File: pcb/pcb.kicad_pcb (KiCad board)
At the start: 2 copper layers, 229.9 x 97.8 mm, 145 parts, among them J1 USB_C_Receptacle_USB2.0, SW1 Reset, SW10 SW_Push, SW11 SW_Push, SW12 SW_Push, SW13 SW_Push, SW14 SW_Push, SW15 SW_Push, SW16 SW_Push, SW17 SW_Push, SW18 SW_Push, SW19 SW_Push, SW2 SW_Push, SW20 SW_Push, SW21 SW_Push, SW22 SW_Push, SW23 SW_Push, SW24 SW_Push, SW25 SW_Push, SW26 SW_Push, SW27 SW_Push, SW28 SW_Push, SW29 SW_Push, SW3 SW_Push, SW30 SW_Push, SW31 SW_Push, SW32 SW_Push, SW33 SW_Push, SW34 SW_Push, SW35 SW_Push, SW36 SW_Push, SW37 SW_Push, SW38 SW_Push, SW39 SW_Push, SW4 SW_Push, SW40 SW_Push, SW41 SW_Push, SW42 SW_Push, SW43 SW_Push, SW44 SW_Push, SW45 SW_Push, SW46 SW_Push, SW47 SW_Push, SW48 SW_Push, SW49 SW_Push, SW5 SW_Push, SW50 SW_Push, SW51 SW_Push, SW52 SW_Push, SW53 SW_Push, SW54 SW_Push, SW55 SW_Push, SW56 SW_Push, SW57 SW_Push, SW58 SW_Push, SW59 SW_Push, SW6 SW_Push, SW60 SW_Push, SW7 SW_Push, SW8 SW_Push, SW9 SW_Push, U1 ATmega32U4-AU, Y1 TSX3225

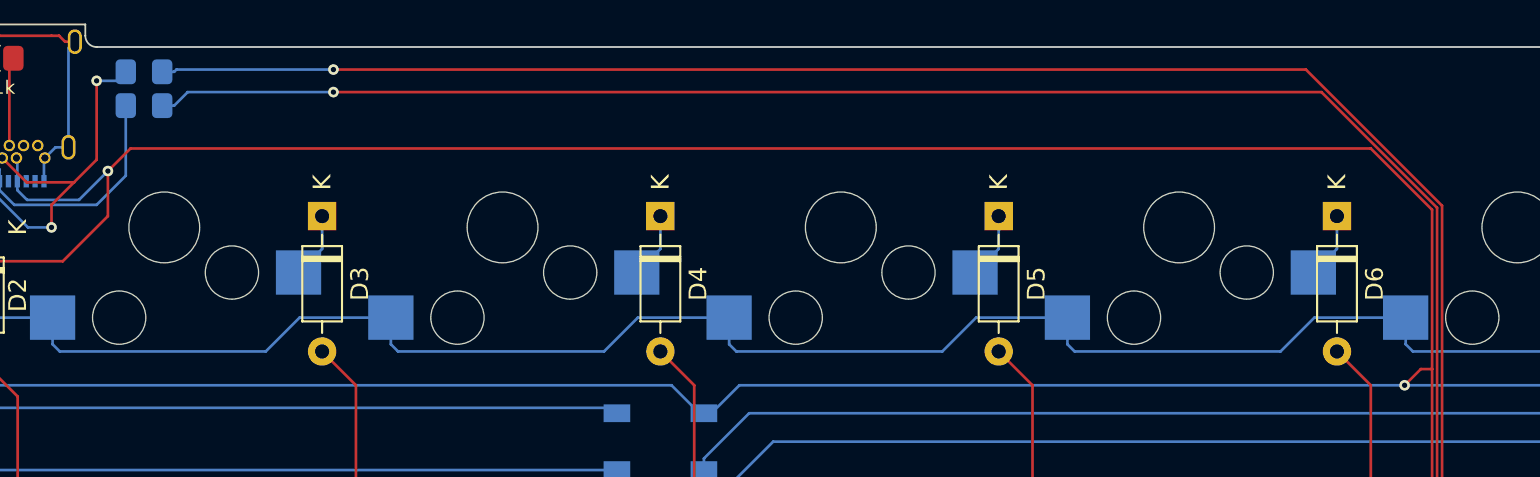
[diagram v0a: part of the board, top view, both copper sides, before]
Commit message: Add a fuse between VBUS and VCC
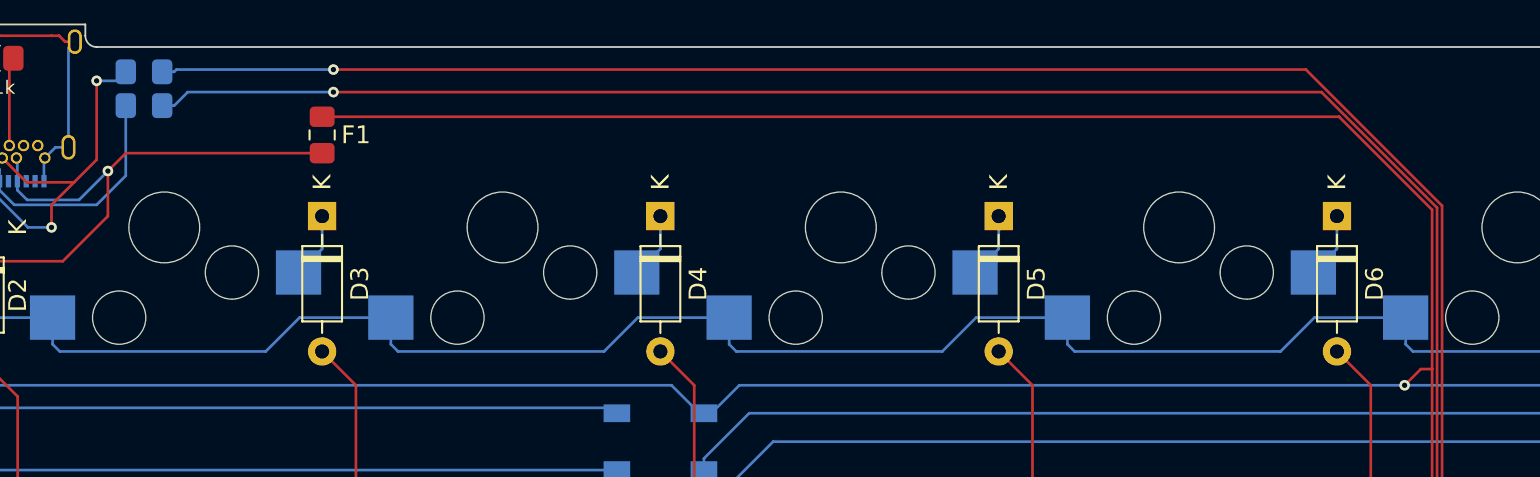
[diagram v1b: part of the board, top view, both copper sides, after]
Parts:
- added F1: 500mA, Fuse:Fuse_0805_2012Metric_Pad1.15x1.40mm_HandSolder, F.Cu at (85.1, 34.2)
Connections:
- C1 pad 1: VBUS -> VCC
- C2 pad 1: VBUS -> VCC
- C3 pad 1: VBUS -> VCC
- C4 pad 1: VBUS -> VCC
- C5 pad 1: VBUS -> VCC
- D60 pad 1: VBUS -> VCC
- D61 pad 1: VBUS -> VCC
- D62 pad 1: VBUS -> VCC
- D63 pad 1: VBUS -> VCC
- D64 pad 1: VBUS -> VCC
- D65 pad 1: VBUS -> VCC
- D66 pad 1: VBUS -> VCC
- D67 pad 1: VBUS -> VCC
- R1 pad 2: VBUS -> VCC
- U1 pad 14: VBUS -> VCC
- U1 pad 2: VBUS -> VCC
- U1 pad 24: VBUS -> VCC
- U1 pad 34: VBUS -> VCC
- U1 pad 44: VBUS -> VCC
- U1 pad 7: VBUS -> VCC
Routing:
- net VCC: track 0.00 -> 617.4 mm, vias 0 -> 6
- net VBUS: track 656.5 -> 39.8 mm, vias 7 -> 1

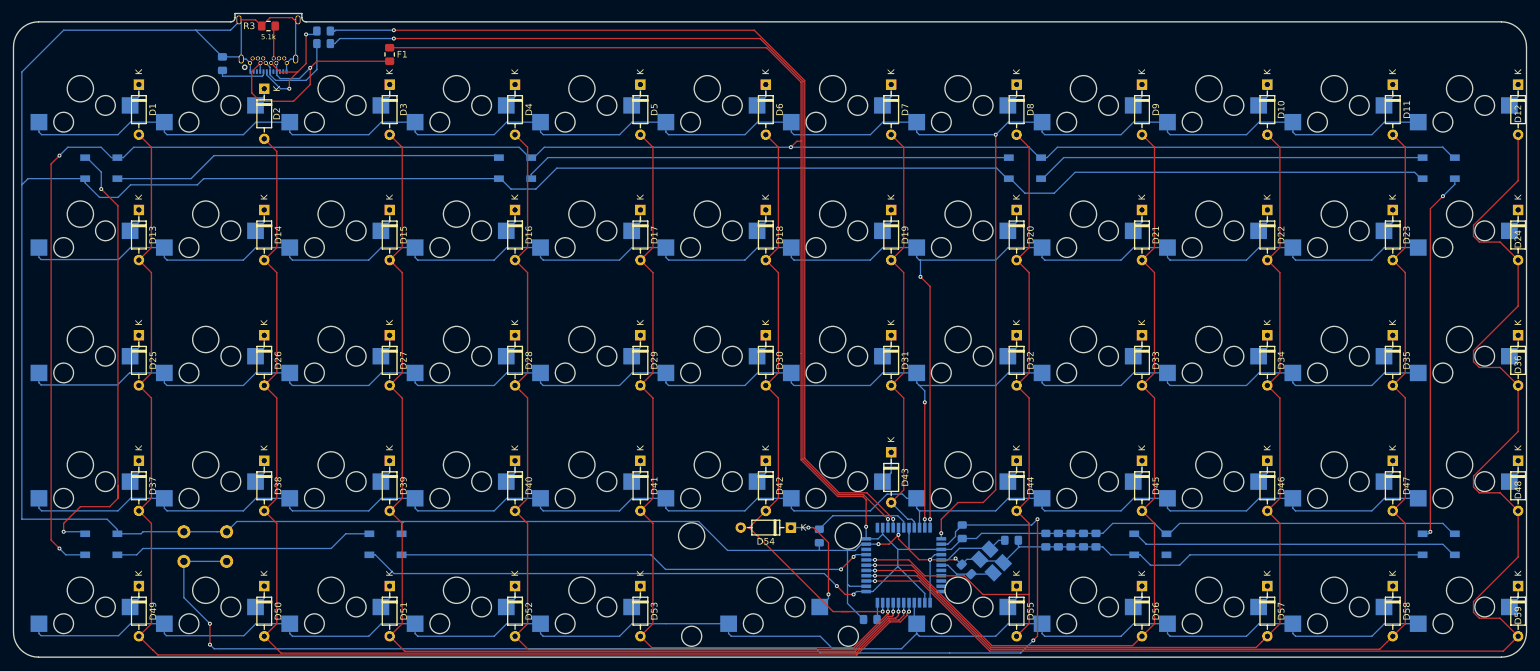
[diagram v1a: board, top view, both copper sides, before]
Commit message: Add decoupling capacitors for LEDs
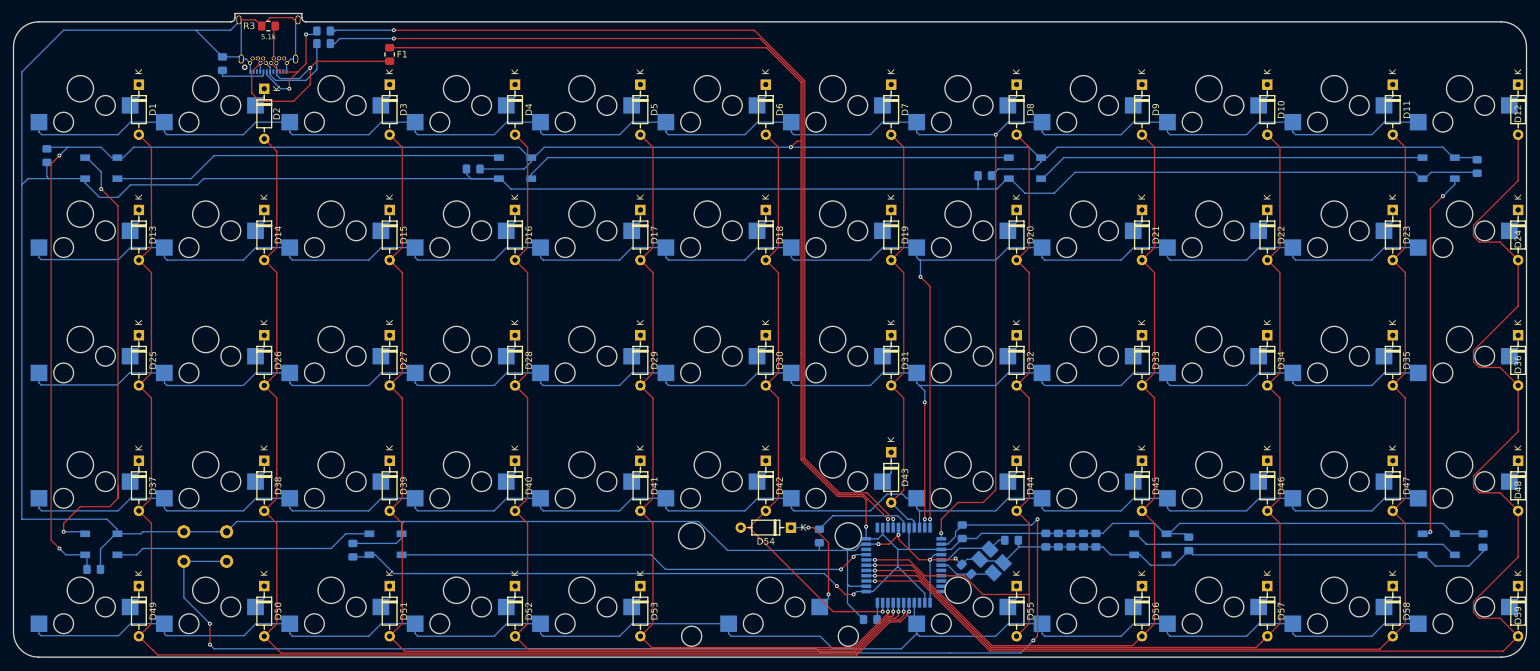
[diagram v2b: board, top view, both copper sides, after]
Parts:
- added C10: 100nF, Capacitor_SMD:C_0805_2012Metric_Pad1.15x1.40mm_HandSolder, B.Cu at (40.1, 112.4)
- added C11: 100nF, Capacitor_SMD:C_0805_2012Metric_Pad1.15x1.40mm_HandSolder, B.Cu at (33.0, 49.5)
- added C12: 100nF, Capacitor_SMD:C_0805_2012Metric_Pad1.15x1.40mm_HandSolder, B.Cu at (97.8, 51.6)
- added C13: 100nF, Capacitor_SMD:C_0805_2012Metric_Pad1.15x1.40mm_HandSolder, B.Cu at (175.5, 52.6)
- added C14: 100nF, Capacitor_SMD:C_0805_2012Metric_Pad1.15x1.40mm_HandSolder, B.Cu at (250.3, 51.2)
- added C15: 100nF, Capacitor_SMD:C_0805_2012Metric_Pad1.15x1.40mm_HandSolder, B.Cu at (251.2, 108.0)
- added C16: 100nF, Capacitor_SMD:C_0805_2012Metric_Pad1.15x1.40mm_HandSolder, B.Cu at (206.5, 108.5)
- added C9: 100nF, Capacitor_SMD:C_0805_2012Metric_Pad1.15x1.40mm_HandSolder, B.Cu at (79.5, 109.5)
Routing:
- net GND: track 614.2 -> 659.3 mm
- net VCC: track 617.4 -> 655.2 mm
